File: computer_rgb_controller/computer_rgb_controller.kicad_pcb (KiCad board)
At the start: 2 copper layers, 80 x 38.1 mm, 22 parts, among them J1 Conn_01x04_Male, J2 Conn_01x04_Female, J3 Conn_01x03_Male, J4 Screw_Terminal_01x02, J5 SJ2-3574A-SMT-TR, Q1 BSS138, Q2 BSS138, Q3 BSS138, SW2 SW_SPST, U1 Particle_Argon

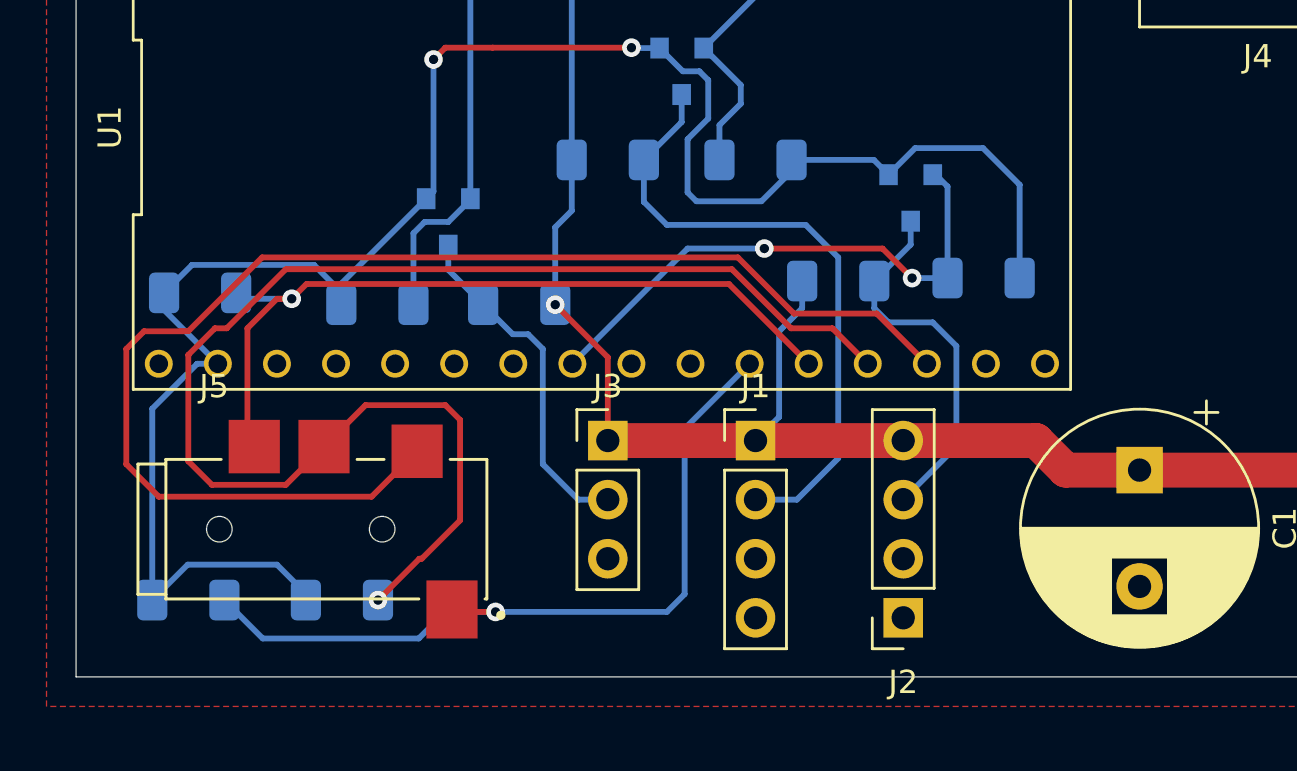
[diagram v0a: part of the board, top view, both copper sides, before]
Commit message: modified connector location to avoid clerance issues
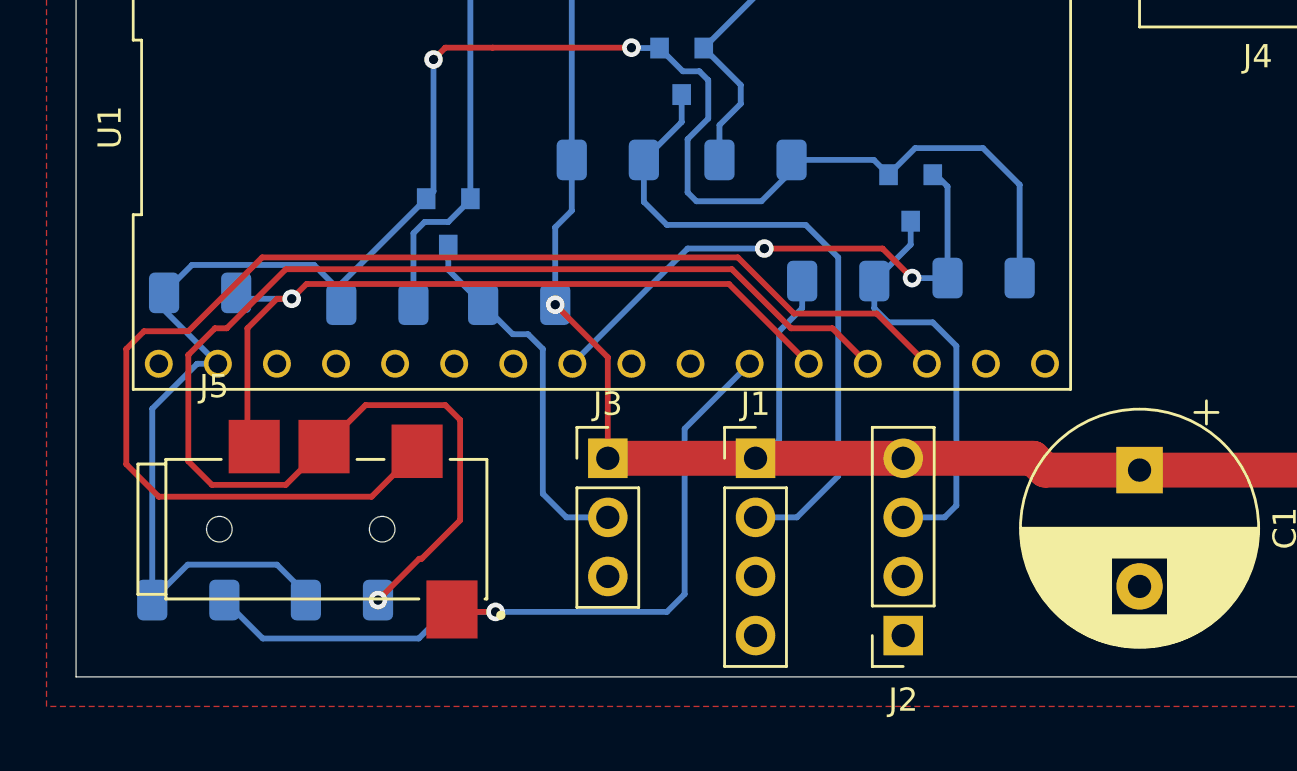
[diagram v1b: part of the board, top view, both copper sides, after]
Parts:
- moved J1 0.76 mm to (106.7, 63.0)
- moved J2 0.76 mm to (113.0, 70.6)
- moved J3 0.76 mm to (100.3, 63.0)
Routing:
- net RGB_D_5V_3: track 16.1 -> 17.9 mm
- net VCC: track 100.0 -> 101.3 mm
- net RGB_D_5V_2: track 14.9 -> 16.0 mm
- net RGB_D_5V_1: track 27.6 -> 28.3 mm

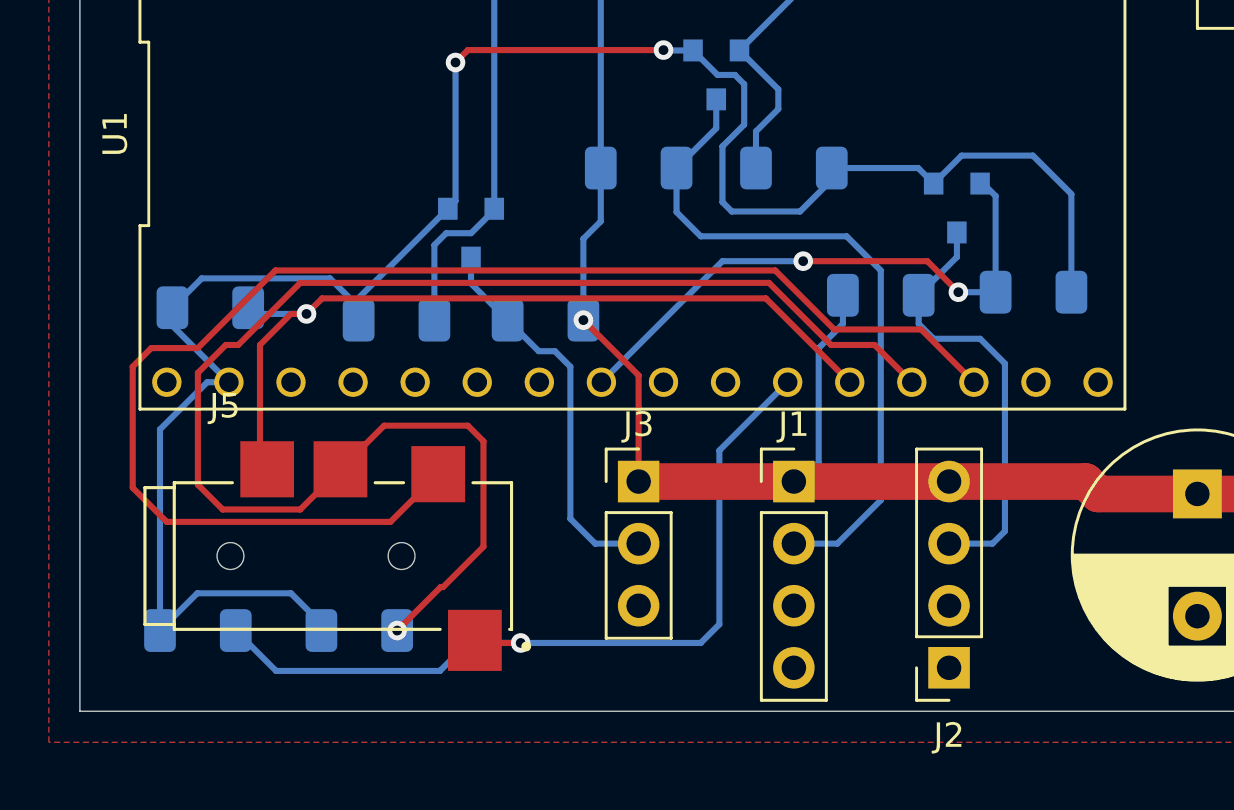
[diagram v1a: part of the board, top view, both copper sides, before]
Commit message: updated trrs jack, old one was out of stock :(
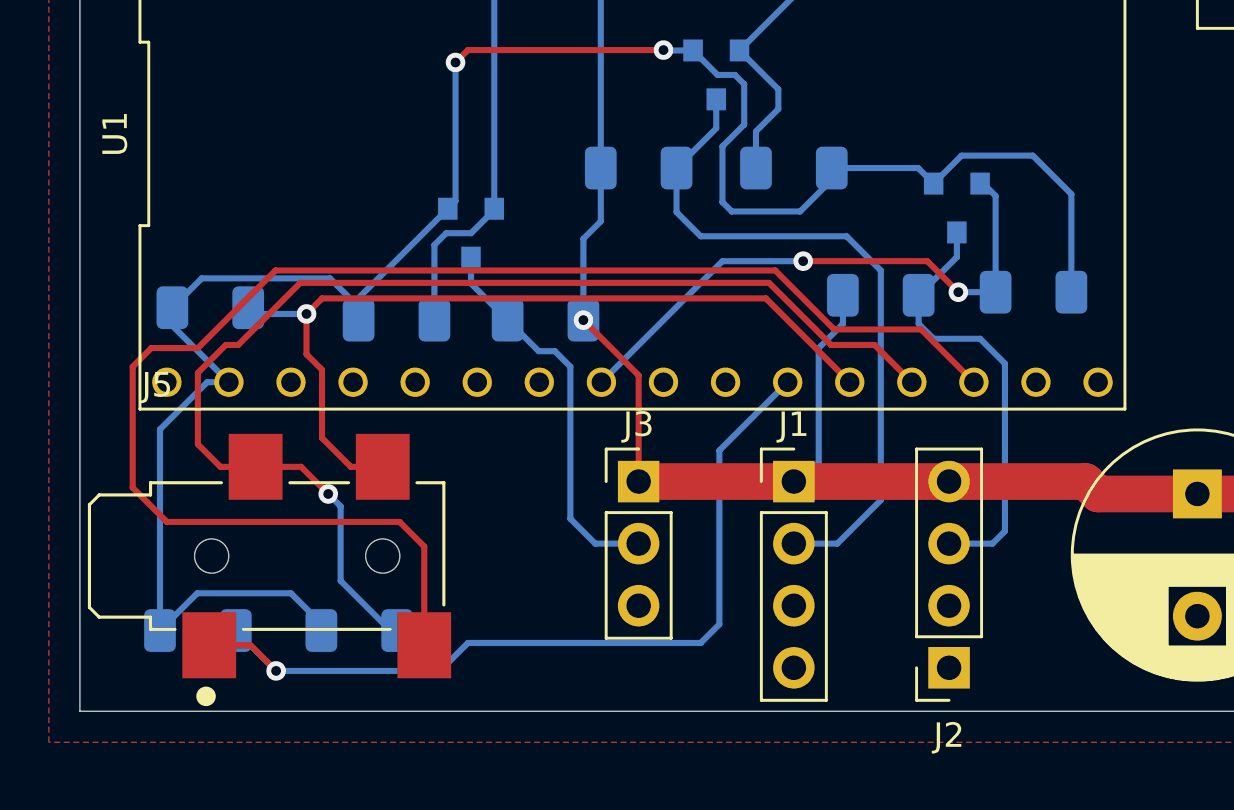
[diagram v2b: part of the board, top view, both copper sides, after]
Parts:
- J5: footprint extra:CUI_SJ2-3574A-SMT-TR -> extra:CUI_SJ2-35043A-SMT-TR
- moved J5 1.27 mm to (86.4, 66.0)
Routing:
- net Net-(J5-Pad3): track 60.0 -> 48.4 mm
- net Net-(J5-Pad2): track 56.8 -> 59.9 mm
- net Net-(J5-Pad1): track 34.2 -> 35.5 mm
- net Net-(J5-Pad4): track 34.0 -> 34.7 mm

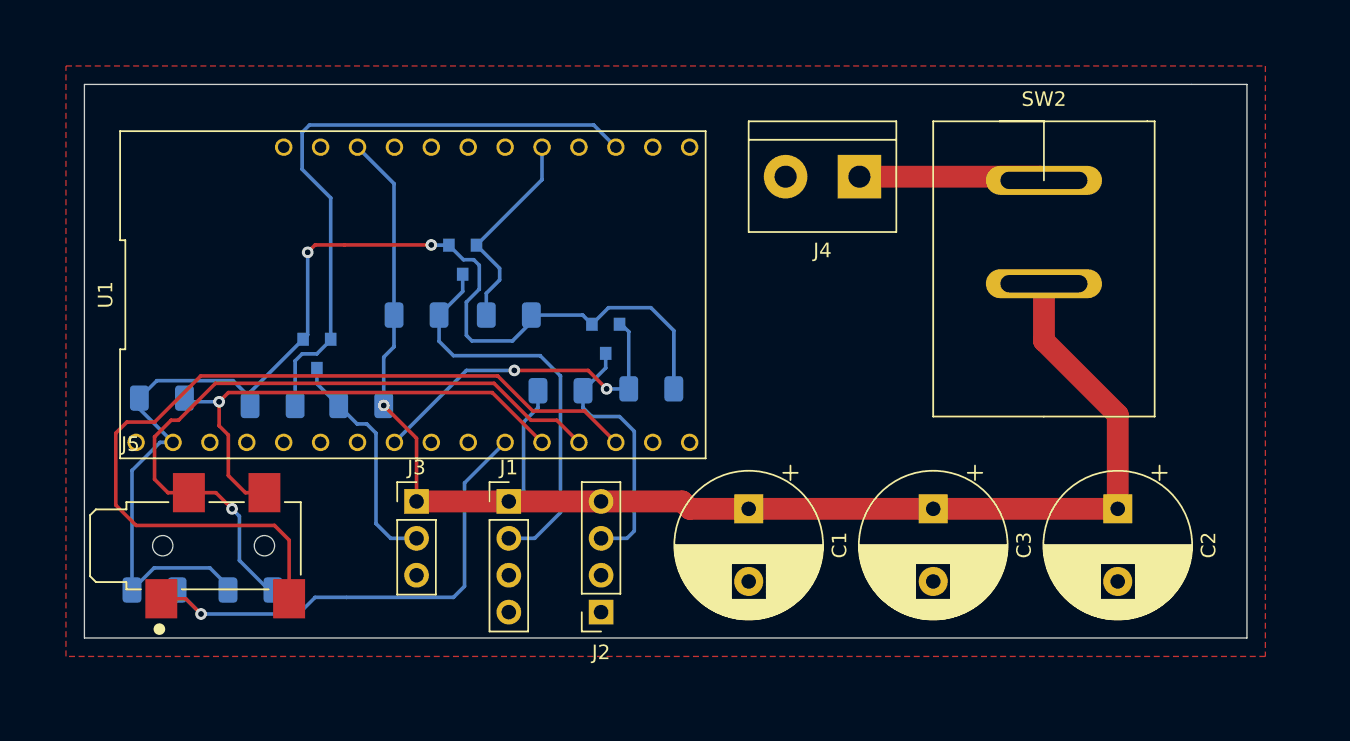
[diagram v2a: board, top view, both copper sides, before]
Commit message: updated TRRS jack bc previous one was wrong one
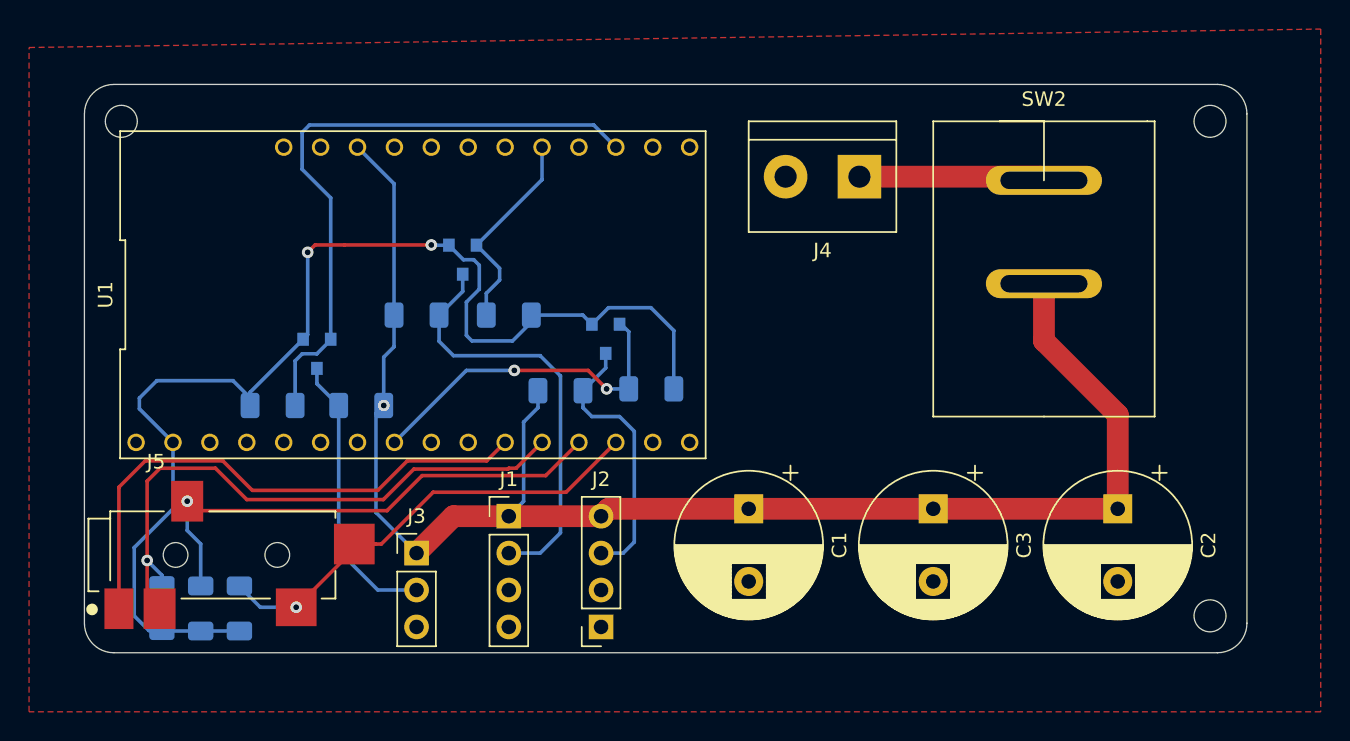
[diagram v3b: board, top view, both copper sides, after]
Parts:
- added REF**: MountingHole_2.2mm_M2, MountingHole:MountingHole_2.2mm_M2, F.Cu at (154.9, 70.9)
- added REF**: MountingHole_2.2mm_M2, MountingHole:MountingHole_2.2mm_M2, F.Cu at (154.9, 36.8)
- added REF**: MountingHole_2.2mm_M2, MountingHole:MountingHole_2.2mm_M2, F.Cu at (80.0, 36.8)
- J5: value SJ2-3574A-SMT-TR -> SJ-43515TS-SMT; footprint extra:CUI_SJ2-35043A-SMT-TR -> extra:CUI_SJ-43515TS-SMT
- moved R8 14.5 mm to (82.8, 70.3), turned to 270 degrees
- moved R7 5.98 mm to (88.1, 70.4), turned to 270 degrees
- moved R9 3.66 mm to (85.5, 70.4), turned to 270 degrees
- moved J3 3.56 mm to (100.3, 66.5)
- moved J2 1.02 mm to (113.0, 71.6)
- moved J1 1.02 mm to (106.7, 64.0)
- moved J5 0.90 mm to (87.0, 66.7)
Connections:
- R7 pad 1: Net-(J5-Pad1) -> Net-(J5-Pad2)
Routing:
- net Net-(J5-Pad2): track 59.9 -> 32.9 mm, vias 0 -> 1
- net Net-(J5-Pad3): track 48.4 -> 35.4 mm
- net Net-(J5-Pad4): track 34.7 -> 41.4 mm
- net VCC: track 101.3 -> 107.2 mm
- net RGB_D_5V_2: track 16.0 -> 19.7 mm
- net Net-(J5-Pad1): track 35.5 -> 37.9 mm, vias 1 -> 0
- net RGB_D_5V_1: track 28.3 -> 29.6 mm
- net 3V3: track 84.1 -> 84.9 mm
- net RGB_D_5V_3: track 17.9 -> 18.8 mm
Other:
- board size 80 x 38.1 mm -> 80 x 39.1 mm
